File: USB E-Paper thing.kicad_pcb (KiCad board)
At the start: 2 copper layers, 79 x 36.7 mm, 97 parts, among them J3 EXTRA2, J4 DOWNSTREAM, J5 SWD, J6 USB 2.0 right angle, J8 POWER_MEASUREMENT, J9 SPI, Q1 AO3400A, Q2 AO3401A, Q3 AO3400A, SW1 BUTTON0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

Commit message: WIP
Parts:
- C1, C2: value 8pF -> 20pF
- D10, D11, D12: value MBR0530 -> B5819W
- R14: footprint Resistor_SMD:R_0402_1005Metric -> Resistor_SMD:R_0603_1608Metric
- R2: value 27 -> 33
- R5: value 68 -> 50
- TH1: footprint Capacitor_SMD:C_1206_3216Metric -> Resistor_THT:R_Axial_DIN0204_L3.6mm_D1.6mm_P5.08mm_Horizontal
- Y1: value 24 MHz -> 12 MHz; footprint Crystal:Crystal_SMD_2520-4Pin_2.5x2.0mm -> Crystal:Crystal_SMD_3225-4Pin_3.2x2.5mm
- moved TH1 4.63 mm to (136.6, 112.6), turned to -90 degrees
- moved C2 1.39 mm to (146.3, 111.7)
- moved C1 1.39 mm to (148.5, 109.3)
- moved Y1 1.39 mm to (149.0, 112.0)
- moved R28 0.91 mm to (113.1, 120.7)
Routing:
- net +BATT: track 100.6 -> 90.9 mm
- net Net-(D9-K): track 13.6 -> 8.86 mm
- net Net-(U3-TEMP): track 75.1 -> 77.9 mm
- net Net-(U1-PH1): track 6.03 -> 7.68 mm
- net GND: track 78.8 -> 77.8 mm, vias 53 -> 52
- net /BUSY_DBG: track 53.1 -> 54.1 mm
- net /BUSY: track 36.0 -> 35.2 mm
- net /PB5: track 15.1 -> 14.6 mm

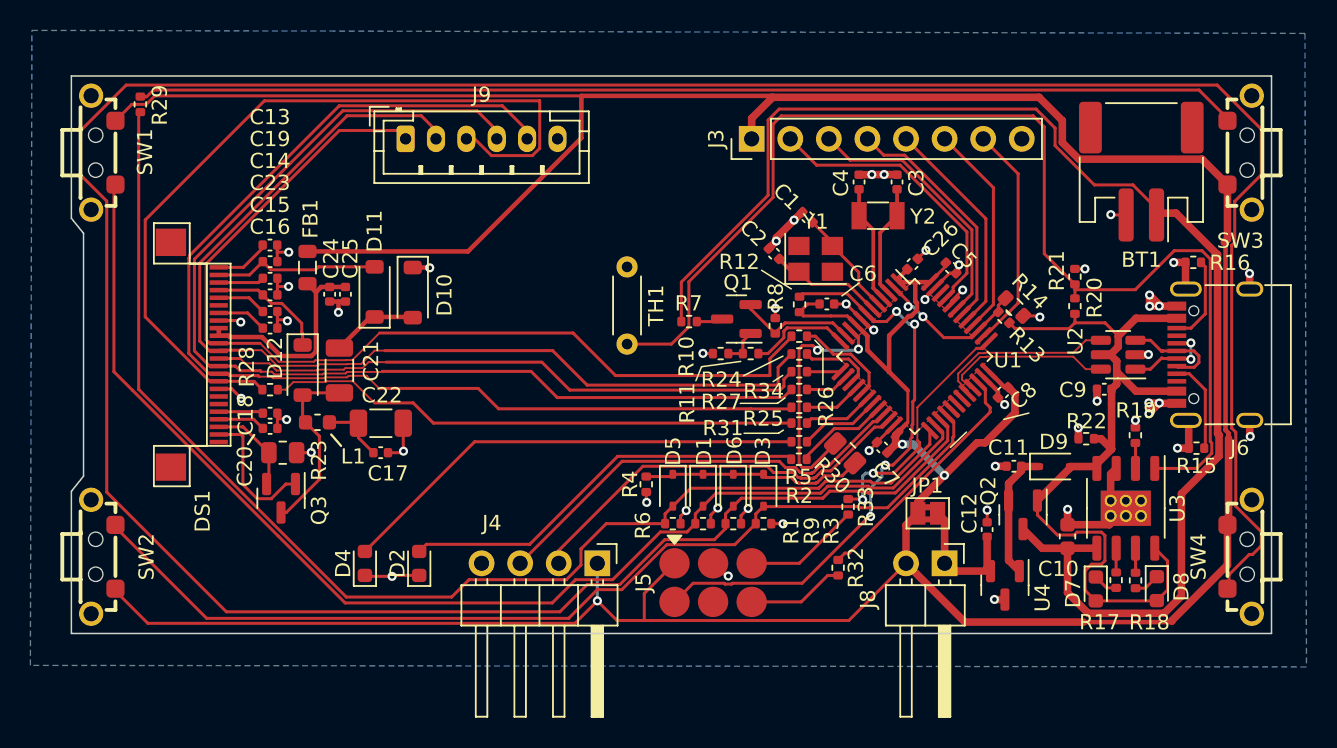
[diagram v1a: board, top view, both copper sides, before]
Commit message: Use single FPC connector for debug signals and downstream
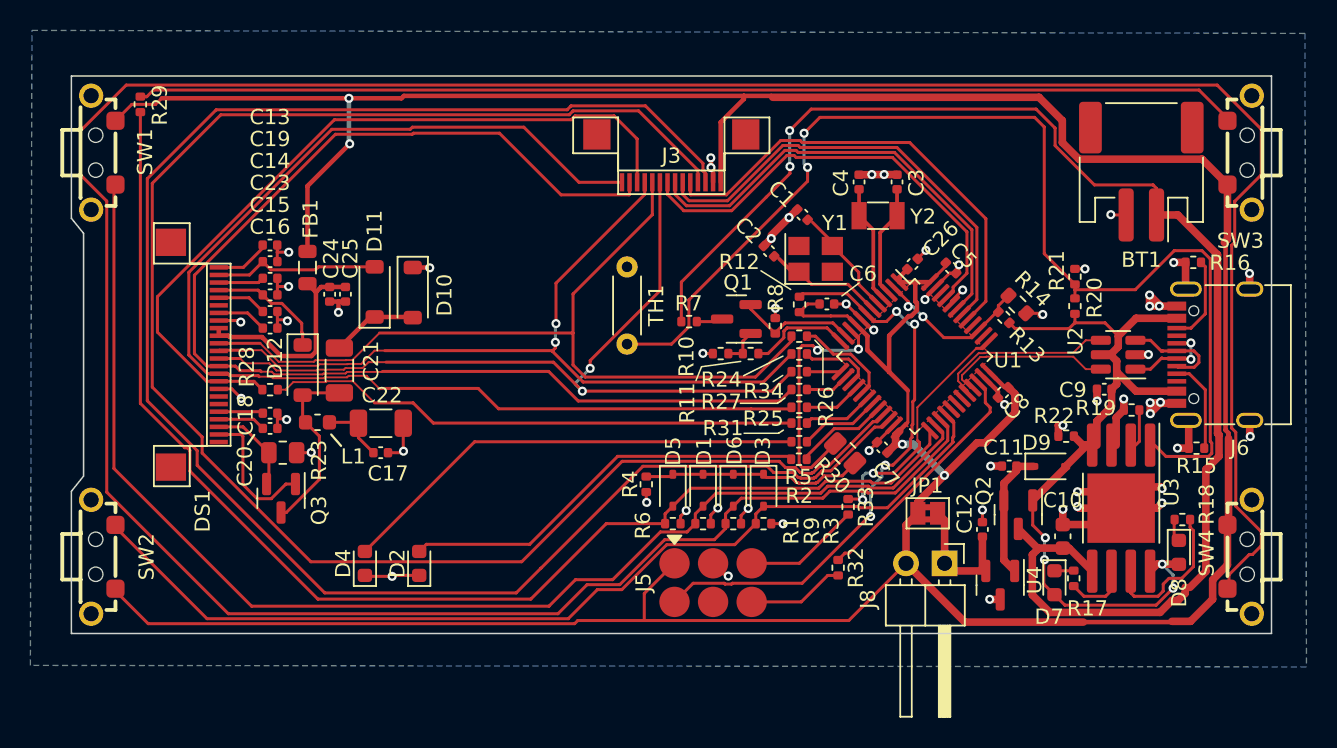
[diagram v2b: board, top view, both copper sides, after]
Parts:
- removed J4: DOWNSTREAM, Connector_PinHeader_2.54mm:PinHeader_1x04_P2.54mm_Horizontal
- removed J9: SPI, Connector_JST:JST_PH_B6B-PH-K_1x06_P2.00mm_Vertical
- J3: footprint Connector_PinHeader_2.54mm:PinHeader_1x08_P2.54mm_Vertical -> local:FPC_14
- U3: footprint local:ESOP-8 -> Package_SO:SOP-8-1EP_4.57x4.57mm_P1.27mm_EP4.57x4.45mm
- moved J3 6.01 mm to (139.5, 107.0), turned to 180 degrees
- moved R18 5.06 mm to (173.1, 129.2), turned to 0 degrees
- moved D8 2.80 mm to (172.9, 131.4)
- moved R17 2.79 mm to (166.0, 133.1), turned to -90 degrees
- moved D7 2.75 mm to (164.7, 133.4)
- moved R19 1.68 mm to (169.8, 122.0), turned to 180 degrees
- moved R22 1.33 mm to (165.5, 123.7)
- moved C1 0.37 mm to (148.1, 109.1)
- moved C2 0.37 mm to (145.9, 111.5)
- moved C12 0.31 mm to (160.0, 129.8)
- moved U3 0.31 mm to (169.1, 128.4)
- moved C10 0.31 mm to (165.3, 130.3)
- moved C11 0.31 mm to (161.7, 125.7)
- moved D9 0.31 mm to (164.4, 125.7)
- moved U4 0.31 mm to (161.1, 133.5)
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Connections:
- J3 pad 2: /PB8 -> GND
- J3 pad 3: /PB7 -> /SERIAL_RX
- J3 pad 4: /PB6 -> /SERIAL_TX
- J3 pad 6: /PB4 -> /PB6
- J3 pad 7: /PA15 -> /PB7
- J3 pad 8: GND -> /PB8
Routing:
- net /SERIAL_RX: track 26.8 -> 116.0 mm
- net /SERIAL_TX: track 28.6 -> 111.9 mm
- net /PB5: track 14.6 -> 31.0 mm
- net /~{CS}: track 39.8 -> 55.8 mm, vias 0 -> 2
- net /PA15: track 14.9 -> 0.00 mm
- net /PB6: track 15.7 -> 30.2 mm
- net /PB4: track 14.2 -> 0.00 mm
- net /SCLK: track 67.7 -> 53.8 mm, vias 0 -> 2
- net GND: track 77.8 -> 90.6 mm, vias 52 -> 58
- net +3V0: track 265.2 -> 252.8 mm, vias 3 -> 4
- net /PB7: track 17.5 -> 29.9 mm
- net /PB8: track 19.1 -> 29.5 mm
- net /MOSI: track 64.6 -> 54.8 mm
- net /D/~{C}: track 71.5 -> 81.2 mm
- net Net-(U3-~{CHRG}): track 1.62 -> 9.91 mm
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
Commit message: switch to JLCPCB version of USBC connect fp
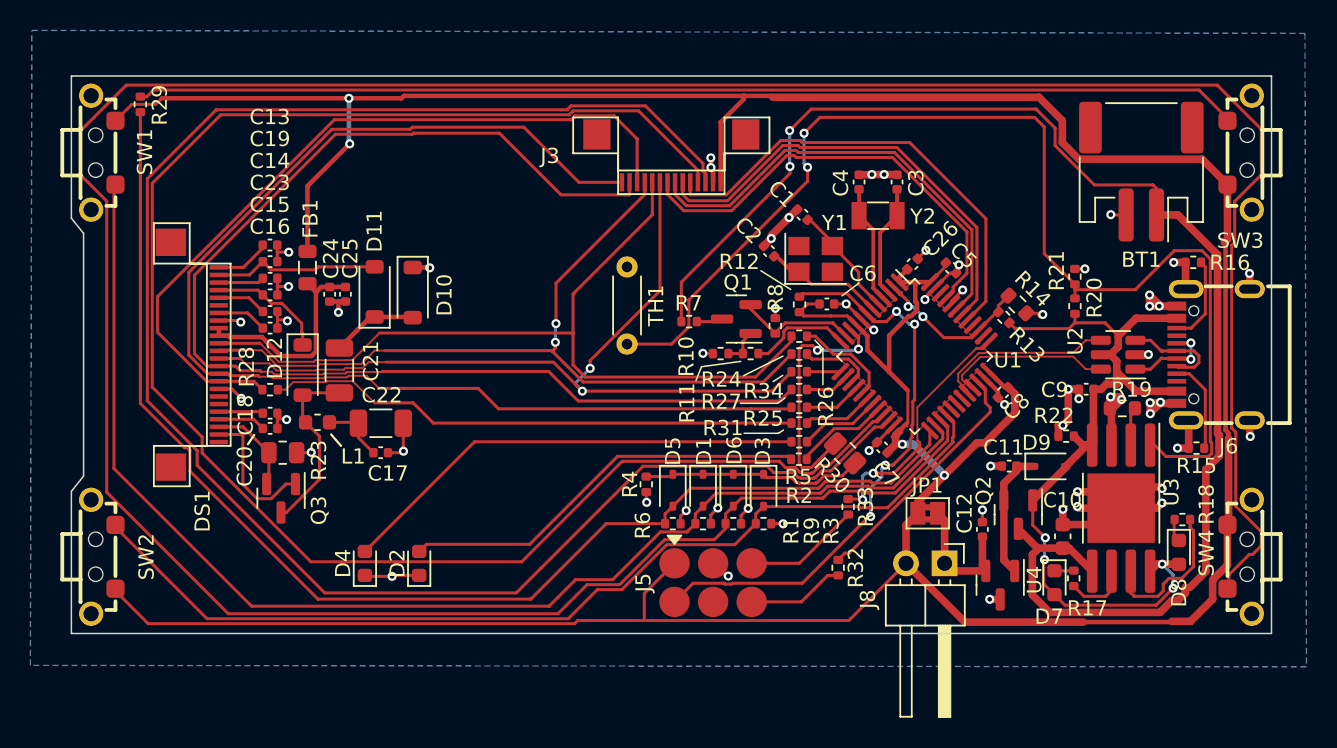
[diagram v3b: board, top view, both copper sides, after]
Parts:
- J6: footprint Connector_USB:USB_C_Receptacle_G-Switch_GT-USB-7010ASV -> local:USB-C-SMD_G-SWITCH_GT-USB-7010ASV
- R19: value ? -> 18k; footprint Resistor_SMD:R_0402_1005Metric -> Resistor_SMD:R_0603_1608Metric
- R20: value ? -> 5k1
- R21: value ? -> 100k
- moved J6 1.33 mm to (175.2, 118.3)
- moved C9 1.19 mm to (166.8, 120.6)
- moved R19 0.62 mm to (169.2, 121.9)
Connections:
- U1 pad 38: /PA15 -> unconnected-(U1-PA15-Pad38)
- U1 pad 40: /PB4 -> unconnected-(U1-PB4-Pad40)
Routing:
- net GND: track 90.6 -> 96.2 mm, vias 58 -> 60
- net /VBUS: track 52.0 -> 52.8 mm

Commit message: Fix all DRC violations, fix 12 MHz crystal connections
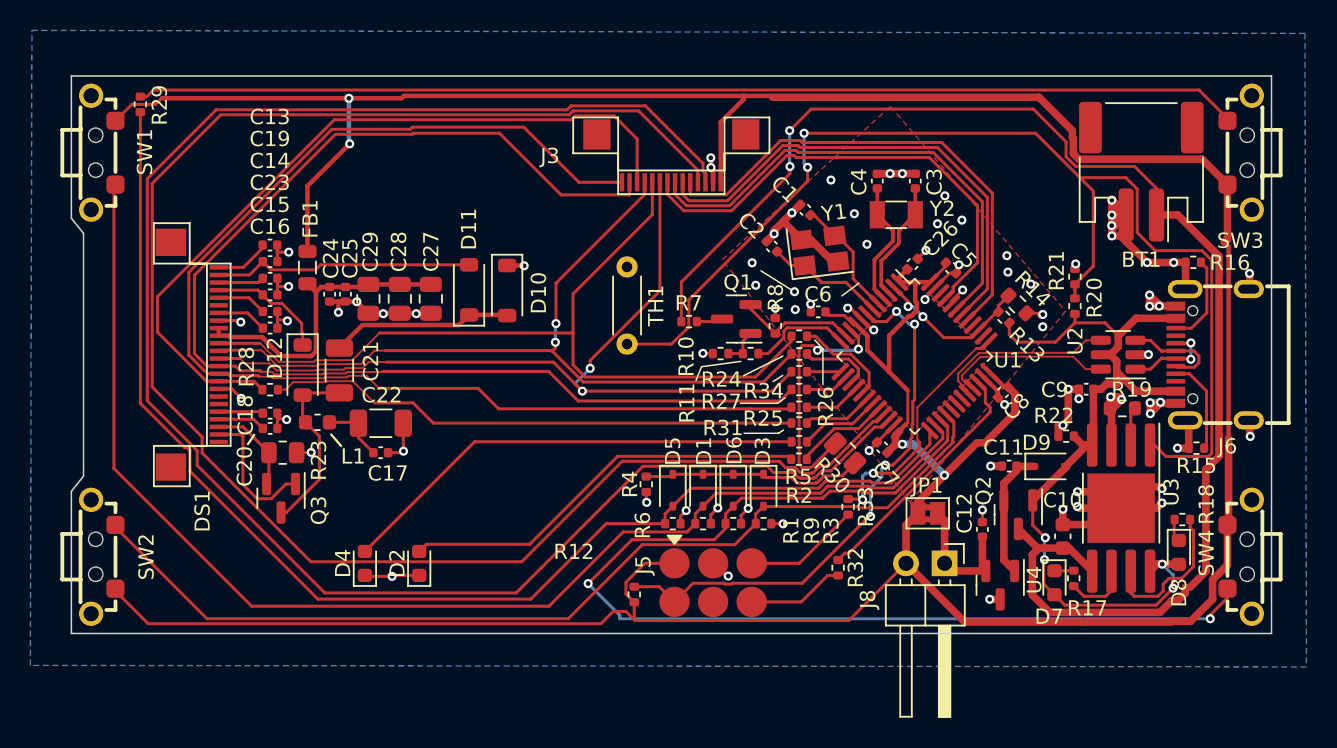
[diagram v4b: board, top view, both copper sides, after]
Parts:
- added C27: 47u/6V, Capacitor_SMD:C_0805_2012Metric, F.Cu at (123.7, 114.7)
- added C28: 47u/6V, Capacitor_SMD:C_0805_2012Metric, F.Cu at (121.6, 114.7)
- added C29: 47u/6V, Capacitor_SMD:C_0805_2012Metric, F.Cu at (119.5, 114.7)
- moved R12 22.0 mm to (137.1, 134.1)
- moved D10 6.22 mm to (128.7, 114.1)
- moved D11 6.22 mm to (126.2, 114.1)
- moved C3 1.20 mm to (155.6, 106.9)
- moved C4 1.20 mm to (153.1, 106.9)
- moved Y2 1.20 mm to (154.3, 109.1)
- moved C6 0.77 mm to (149.2, 115.5), turned to 180 degrees
- moved Y1 0.60 mm to (149.3, 111.5), turned to 7 degrees
- moved C1 0.36 mm to (148.3, 108.8)
- moved C2 0.36 mm to (146.1, 111.2)
- moved J6 0.06 mm to (175.1, 118.3)
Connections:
- Y1 pad 2: unconnected-(Y1-Pad2) -> GND
- Y1 pad 4: unconnected-(Y1-Pad4) -> GND
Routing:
- net /BUTTON3: track 203.2 -> 74.3 mm, vias 0 -> 2
- net GND: track 96.2 -> 120.2 mm, vias 60 -> 82
- net Net-(D10-A): track 5.70 -> 12.2 mm
- net /E-Ink display/PREVGL: track 10.9 -> 17.2 mm
- net /E-Ink display/VCC: track 14.4 -> 20.0 mm
- net /PB6: track 30.2 -> 32.3 mm
- net /PB7: track 29.9 -> 32.0 mm
- net /NRST: track 38.5 -> 36.4 mm
- net /PB8: track 29.5 -> 31.5 mm
- net Net-(U3-TEMP): track 76.4 -> 78.2 mm
- net /PB5: track 31.0 -> 32.6 mm
- net /VBUS: track 52.8 -> 54.0 mm
- net +3V0: track 252.8 -> 251.9 mm
- net Net-(U1-PH0): track 7.13 -> 7.89 mm
- net Net-(U1-PC15): track 7.84 -> 8.41 mm
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- added copper zone on F.Cu, net GND
